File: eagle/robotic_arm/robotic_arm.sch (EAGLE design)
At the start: 98 parts, among them J2 (ID,OD)=(2.1,5.5)MM, SW1 5A/28V, Y1 16MHz

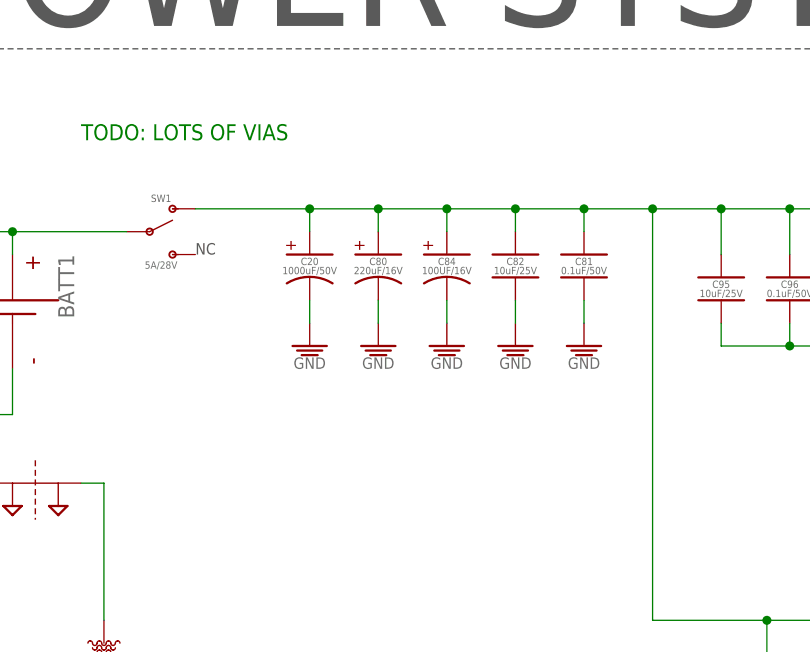
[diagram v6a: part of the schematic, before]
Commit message: Moved DEMUX to give some more power plane area.
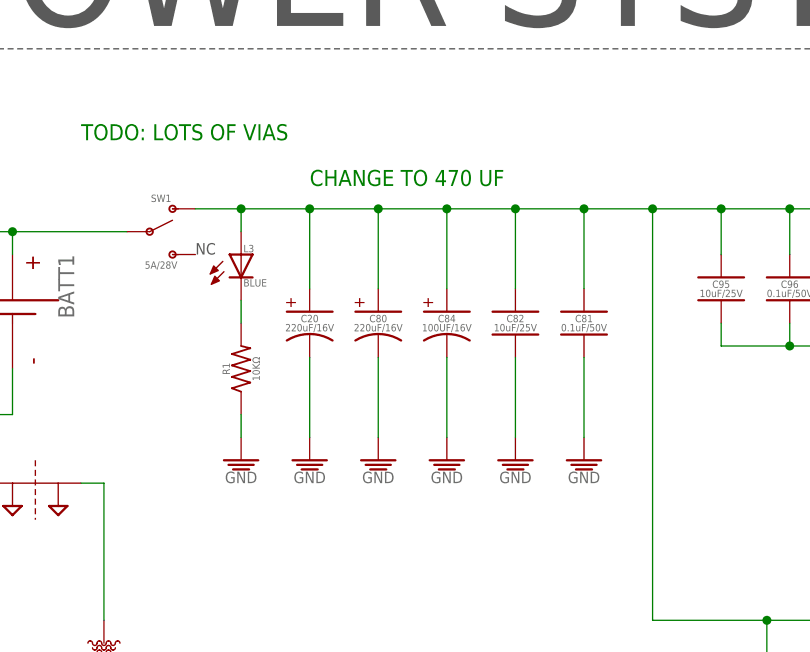
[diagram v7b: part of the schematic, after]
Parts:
- added L3: BLUE, MrSwirlyEyes:LED_SMD-805_DISCRETE_BLUE
- added R1: 10KΩ, MrSwirlyEyes:RESISTORSMD-0805_1/8W_10K_5%
- C20: value 1000uF/50V -> 220uF/16V; device MrSwirlyEyes:CAP_POLARIZED_ALUM-ELECTROLYTIC_PTH_1000UF-50V-20% -> MrSwirlyEyes:CAP_POLARIZED_ALUM-ELECTROLYTIC_SMD_220UF-16V-20%
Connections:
- new net N$2: L3.K, R1.2
- net GND: now also R1.1
- net N$1: now also L3.A
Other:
- note added: "CHANGE TO 470 UF"
- moved on the sheet: C20, C80, C81, C82, C84
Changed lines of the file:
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@@
 <setting verticaltext="up"/>
 </settings>
-<grid distance="0.1" unitdist="inch" unit="inch" style="lines" multiple="1" display="no" altdistance="0.01" altunitdist="inch" altunit="inch"/>
+<grid distance="0.1" unitdist="inch" unit="inch" style="lines" multiple="1" display="no" altdistance="0.05" altunitdist="inch" altunit="inch"/>
 <layers>
 <layer number="1" name="Top" color="4" fill="1" visible="no" active="no"/>
@@
 <part name="SUPPLY37" library="MrSwirlyEyes" deviceset="5V" device=""/>
 <part name="J2" library="MrSwirlyEyes" deviceset="POWER_JACK-BARREL_ID2.1MM-OD5.5MM" device="" value="(ID,OD)=(2.1,5.5)MM"/>
-<part name="C20" library="MrSwirlyEyes" deviceset="CAP_POLARIZED" device="_ALUM-ELECTROLYTIC_PTH_1000UF-50V-20%" value="1000uF/50V"/>
+<part name="C20" library="MrSwirlyEyes" deviceset="CAP_POLARIZED" device="_ALUM-ELECTROLYTIC_SMD_220UF-16V-20%" value="220uF/16V"/>
 <part name="GND4" library="MrSwirlyEyes" deviceset="GND" device=""/>
 <part name="VREG1" library="MrSwirlyEyes" deviceset="VREG_MIC29501-5.0_LINEAR_ULDO_5A-5V" device="MIC29501-5.0_5A-5V" value="5A/5V"/>
@@
 <part name="SUPPLY51" library="SparkFun-PowerSymbols" deviceset="2PT_GND_TIE" device=""/>
 <part name="SUPPLY52" library="SparkFun-PowerSymbols" deviceset="2PT_GND_TIE" device=""/>
+<part name="L3" library="MrSwirlyEyes" deviceset="LED" device="_SMD-805_DISCRETE_BLUE" value="BLUE"/>
+<part name="R1" library="MrSwirlyEyes" deviceset="RESISTOR" device="SMD-0805_1/8W_10K_5%" value="10KΩ"/>
+<part name="GND6" library="MrSwirlyEyes" deviceset="GND" device=""/>
 </parts>
 <sheets>
@@
 <text x="287.02" y="269.24" size="1.778" layer="91">WIRE DEMUX</text>
 <text x="177.8" y="182.88" size="1.778" layer="91">TODO: LOTS OF VIAS</text>
+<text x="203.2" y="177.8" size="1.778" layer="91">CHANGE TO 470 UF</text>
 </plain>
 <instances>
@@
 <instance part="GND125" gate="GND" x="274.32" y="154.94"/>
 <instance part="D7" gate="G$1" x="273.05" y="139.7" rot="R90"/>
-<instance part="C80" gate="G$1" x="210.82" y="170.18"/>
-<instance part="C81" gate="G$1" x="233.68" y="170.18"/>
-<instance part="C82" gate="G$1" x="226.06" y="170.18"/>
-<instance part="GND127" gate="GND" x="210.82" y="160.02"/>
-<instance part="GND128" gate="GND" x="226.06" y="160.02"/>
-<instance part="GND129" gate="GND" x="233.68" y="160.02"/>
+<instance part="C80" gate="G$1" x="210.82" y="163.83"/>
+<instance part="C81" gate="G$1" x="233.68" y="163.83"/>
+<instance part="C82" gate="G$1" x="226.06" y="163.83"/>
+<instance part="GND127" gate="GND" x="210.82" y="147.32"/>
+<instance part="GND128" gate="GND" x="226.06" y="147.32"/>
+<instance part="GND129" gate="GND" x="233.68" y="147.32"/>
 <instance part="SUPPLY85" gate="VCC" x="294.64" y="177.8"/>
 <instance part="L1" gate="G$1" x="302.26" y="175.26"/>
 <instance part="C83" gate="G$1" x="287.02" y="121.92"/>
-<instance part="C84" gate="G$1" x="218.44" y="170.18"/>
-<instance part="GND130" gate="GND" x="218.44" y="160.02"/>
+<instance part="C84" gate="G$1" x="218.44" y="163.83"/>
+<instance part="GND130" gate="GND" x="218.44" y="147.32"/>
 <instance part="L2" gate="G$1" x="160.02" y="144.78"/>
 <instance part="C85" gate="G$1" x="309.88" y="167.64"/>
@@
 <instance part="SUPPLY37" gate="5V" x="86.36" y="40.64"/>
 <instance part="J2" gate="G$1" x="142.24" y="170.18"/>
-<instance part="C20" gate="G$1" x="203.2" y="170.18"/>
-<instance part="GND4" gate="GND" x="203.2" y="160.02"/>
+<instance part="C20" gate="G$1" x="203.2" y="163.83"/>
+<instance part="GND4" gate="GND" x="203.2" y="147.32"/>
 <instance part="VREG1" gate="G$1" x="274.32" y="127"/>
 <instance part="S7" gate="G$1" x="200.66" y="340.36"/>
@@
 <instance part="SUPPLY51" gate="G$1" x="144.78" y="144.78"/>
 <instance part="SUPPLY52" gate="G$1" x="172.72" y="144.78"/>
+<instance part="L3" gate="G$1" x="195.58" y="170.18"/>
+<instance part="R1" gate="G$1" x="195.58" y="157.48" rot="R90"/>
+<instance part="GND6" gate="GND" x="195.58" y="147.32"/>
 </instances>
 <busses>
@@
 <segment>
 <pinref part="C80" gate="G$1" pin="K"/>
-<wire x1="210.82" y1="165.1" x2="210.82" y2="162.56" width="0.1524" layer="91"/>
+<wire x1="210.82" y1="158.75" x2="210.82" y2="149.86" width="0.1524" layer="91"/>
 <pinref part="GND127" gate="GND" pin="GND"/>
 </segment>
@@
 <pinref part="C82" gate="G$1" pin="2"/>
 <pinref part="GND128" gate="GND" pin="GND"/>
-<wire x1="226.06" y1="162.56" x2="226.06" y2="165.1" width="0.1524" layer="91"/>
+<wire x1="226.06" y1="149.86" x2="226.06" y2="158.75" width="0.1524" layer="91"/>
 </segment>
 <segment>
 <pinref part="C81" gate="G$1" pin="2"/>
 <pinref part="GND129" gate="GND" pin="GND"/>
-<wire x1="233.68" y1="162.56" x2="233.68" y2="165.1" width="0.1524" layer="91"/>
+<wire x1="233.68" y1="149.86" x2="233.68" y2="158.75" width="0.1524" layer="91"/>
 </segment>
 <segment>
 <pinref part="GND130" gate="GND" pin="GND"/>
 <pinref part="C84" gate="G$1" pin="K"/>
-<wire x1="218.44" y1="162.56" x2="218.44" y2="165.1" width="0.1524" layer="91"/>
+<wire x1="218.44" y1="149.86" x2="218.44" y2="158.75" width="0.1524" layer="91"/>
 </segment>
 <segment>
 <pinref part="C20" gate="G$1" pin="K"/>
-<wire x1="203.2" y1="165.1" x2="203.2" y2="162.56" width="0.1524" layer="91"/>
+<wire x1="203.2" y1="158.75" x2="203.2" y2="149.86" width="0.1524" layer="91"/>
 <pinref part="GND4" gate="GND" pin="GND"/>
 </segment>
@@
 <pinref part="AVR_ISP" gate="G$1" pin="6"/>
 <wire x1="287.02" y1="35.56" x2="284.48" y2="35.56" width="0.1524" layer="91"/>
+</segment>
+<segment>
+<pinref part="R1" gate="G$1" pin="1"/>
+<wire x1="195.58" y1="152.4" x2="195.58" y2="149.86" width="0.1524" layer="91"/>
+<pinref part="GND6" gate="GND" pin="GND"/>
 </segment>
 </net>
@@
 <wire x1="261.62" y1="129.54" x2="261.62" y2="124.46" width="0.1524" layer="91"/>
 <pinref part="SW1" gate="G$1" pin="S1"/>
-<wire x1="190.5" y1="175.26" x2="203.2" y2="175.26" width="0.1524" layer="91"/>
+<wire x1="190.5" y1="175.26" x2="195.58" y2="175.26" width="0.1524" layer="91"/>
+<wire x1="195.58" y1="175.26" x2="203.2" y2="175.26" width="0.1524" layer="91"/>
 <wire x1="203.2" y1="175.26" x2="210.82" y2="175.26" width="0.1524" layer="91"/>
 <wire x1="210.82" y1="175.26" x2="218.44" y2="175.26" width="0.1524" layer="91"/>
@@
 <junction x="241.3" y="175.26"/>
 <pinref part="C81" gate="G$1" pin="1"/>
-<wire x1="233.68" y1="172.72" x2="233.68" y2="175.26" width="0.1524" layer="91"/>
+<wire x1="233.68" y1="166.37" x2="233.68" y2="175.26" width="0.1524" layer="91"/>
 <junction x="233.68" y="175.26"/>
 <pinref part="C82" gate="G$1" pin="1"/>
-<wire x1="226.06" y1="172.72" x2="226.06" y2="175.26" width="0.1524" layer="91"/>
+<wire x1="226.06" y1="166.37" x2="226.06" y2="175.26" width="0.1524" layer="91"/>
 <junction x="226.06" y="175.26"/>
 <pinref part="C80" gate="G$1" pin="A"/>
-<wire x1="210.82" y1="172.72" x2="210.82" y2="175.26" width="0.1524" layer="91"/>
+<wire x1="210.82" y1="166.37" x2="210.82" y2="175.26" width="0.1524" layer="91"/>
 <junction x="210.82" y="175.26"/>
 <pinref part="C84" gate="G$1" pin="A"/>
-<wire x1="218.44" y1="172.72" x2="218.44" y2="175.26" width="0.1524" layer="91"/>
+<wire x1="218.44" y1="166.37" x2="218.44" y2="175.26" width="0.1524" layer="91"/>
 <junction x="218.44" y="175.26"/>
 <pinref part="C96" gate="G$1" pin="1"/>
@@
 <junction x="261.62" y="175.26"/>
 <pinref part="C20" gate="G$1" pin="A"/>
-<wire x1="203.2" y1="172.72" x2="203.2" y2="175.26" width="0.1524" layer="91"/>
+<wire x1="203.2" y1="166.37" x2="203.2" y2="175.26" width="0.1524" layer="91"/>
 <junction x="203.2" y="175.26"/>
 <pinref part="VREG1" gate="G$1" pin="VIN"/>
@@
 <wire x1="264.16" y1="127" x2="264.16" y2="129.54" width="0.1524" layer="91"/>
 <junction x="264.16" y="129.54"/>
+<pinref part="L3" gate="G$1" pin="A"/>
+<wire x1="195.58" y1="172.72" x2="195.58" y2="175.26" width="0.1524" layer="91"/>
+<junction x="195.58" y="175.26"/>
 </segment>
 </net>
@@
 </segment>
 </net>
+<net name="N$2" class="0">
+<segment>
+<pinref part="L3" gate="G$1" pin="K"/>
+<wire x1="195.58" y1="165.1" x2="195.58" y2="162.56" width="0.1524" layer="91"/>
+<pinref part="R1" gate="G$1" pin="2"/>
+</segment>
+</net>
 </nets>
 </sheet>
 </sheets>
+<errors>
+</errors>
 </schematic>
 </drawing>

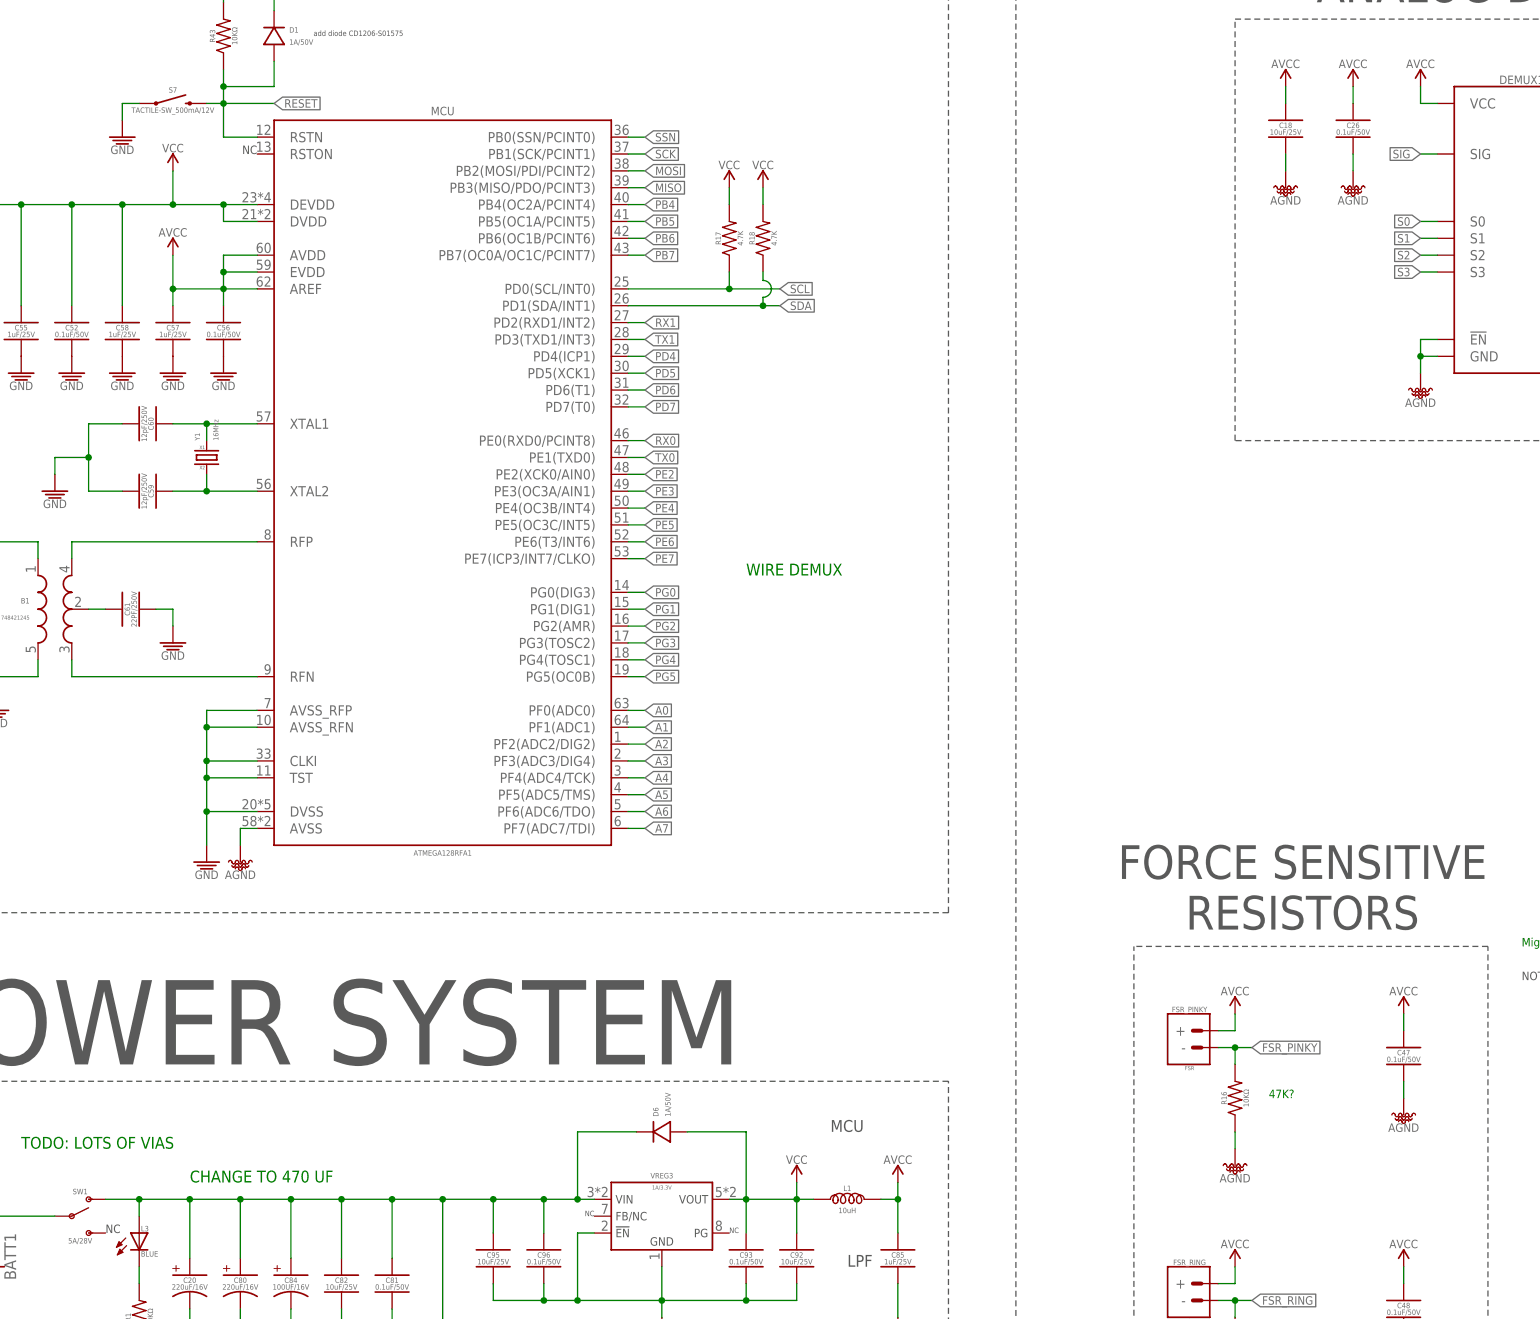
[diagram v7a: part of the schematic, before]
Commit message: Routed VBATT and moved MCU regulator for a well-shaped power plane
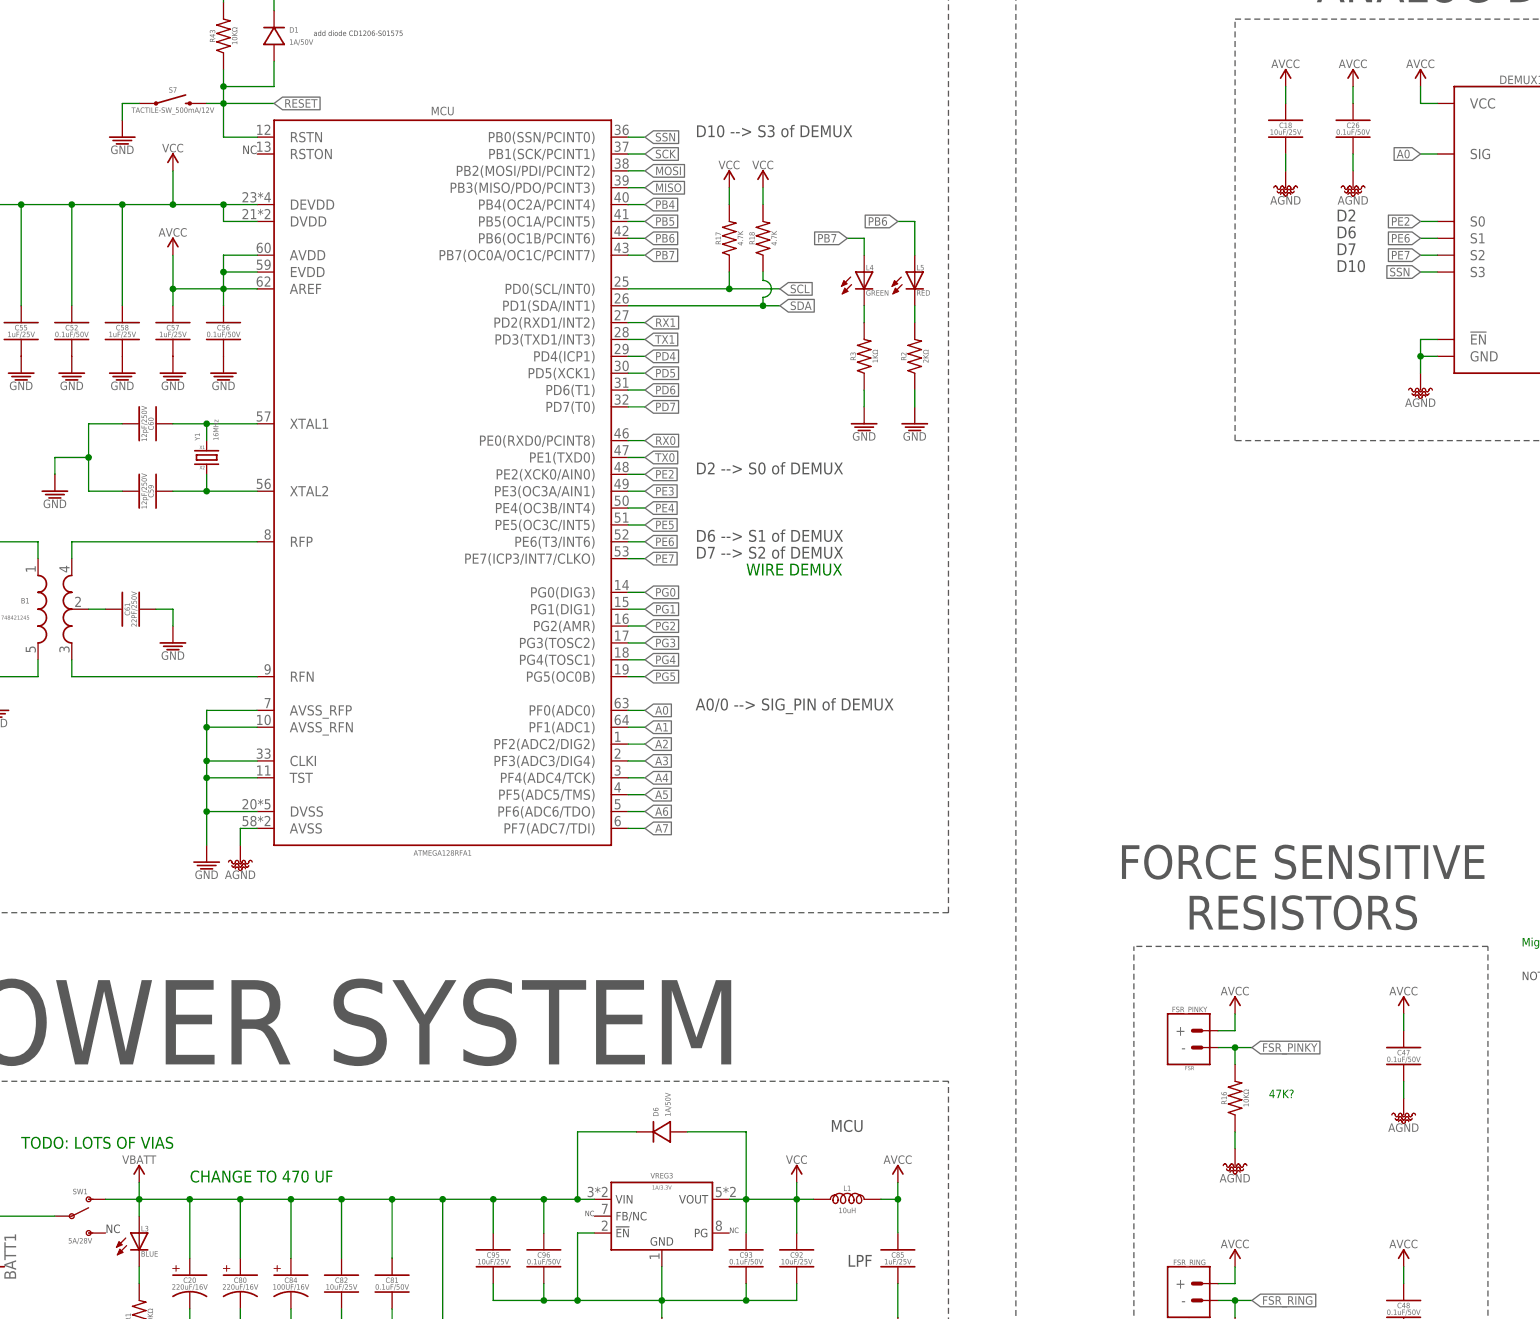
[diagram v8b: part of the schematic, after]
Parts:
- added L4: GREEN, MrSwirlyEyes:LED_SMD-805_DISCRETE_GREEN
- added L5: RED, MrSwirlyEyes:LED_SMD-805_DISCRETE_RED
- added R2: 2KΩ, MrSwirlyEyes:RESISTORSMD-0805_1/8W_2K_5%
- added R3: 1KΩ, MrSwirlyEyes:RESISTORSMD-0805_1/8W_1K_5%
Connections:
- net N$1 renamed VBATT
- removed net S0: DEMUX1.S0
- removed net S1: DEMUX1.S1
- removed net S2: DEMUX1.S2
- removed net S3: DEMUX1.S3
- removed net SIG: DEMUX1.SIG
- new net N$3: L4.K, R3.2
- new net N$5: L5.K, R2.2
- net A0: now also DEMUX1.SIG
- net GND: now also R2.1, R3.1
- net PB6: now also L5.A
- net PB7: now also L4.A
- net PE2: now also DEMUX1.S0
- net PE6: now also DEMUX1.S1
- net PE7: now also DEMUX1.S2
- net SSN: now also DEMUX1.S3
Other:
- note added: "A0/0 --> SIG_PIN of DEMUX"
- note added: "D10"
- note added: "D10 --> S3 of DEMUX"
- note added: "D2"
- note added: "D2 --> S0 of DEMUX"
- note added: "D6"
- note added: "D6 --> S1 of DEMUX"
- note added: "D7"
- note added: "D7 --> S2 of DEMUX"
